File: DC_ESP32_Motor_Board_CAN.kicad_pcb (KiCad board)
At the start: 2 copper layers, 29.8 x 59.4 mm, 32 parts, among them IC1 VNH7100BASTR, IC2 TJA1050T_CM, J1 SM04B-SRSS-TB, J2 SM04B-SRSS-TB, J3 XT30PB, J4 XT30PB, J5 Conn_01x03_Pin, J6 Conn_01x02_Pin, J7 XT30PB, SW1 DSHP04TJGER, U1 MOUDLE-SEEEDUINO-XIAO-ESP32C3

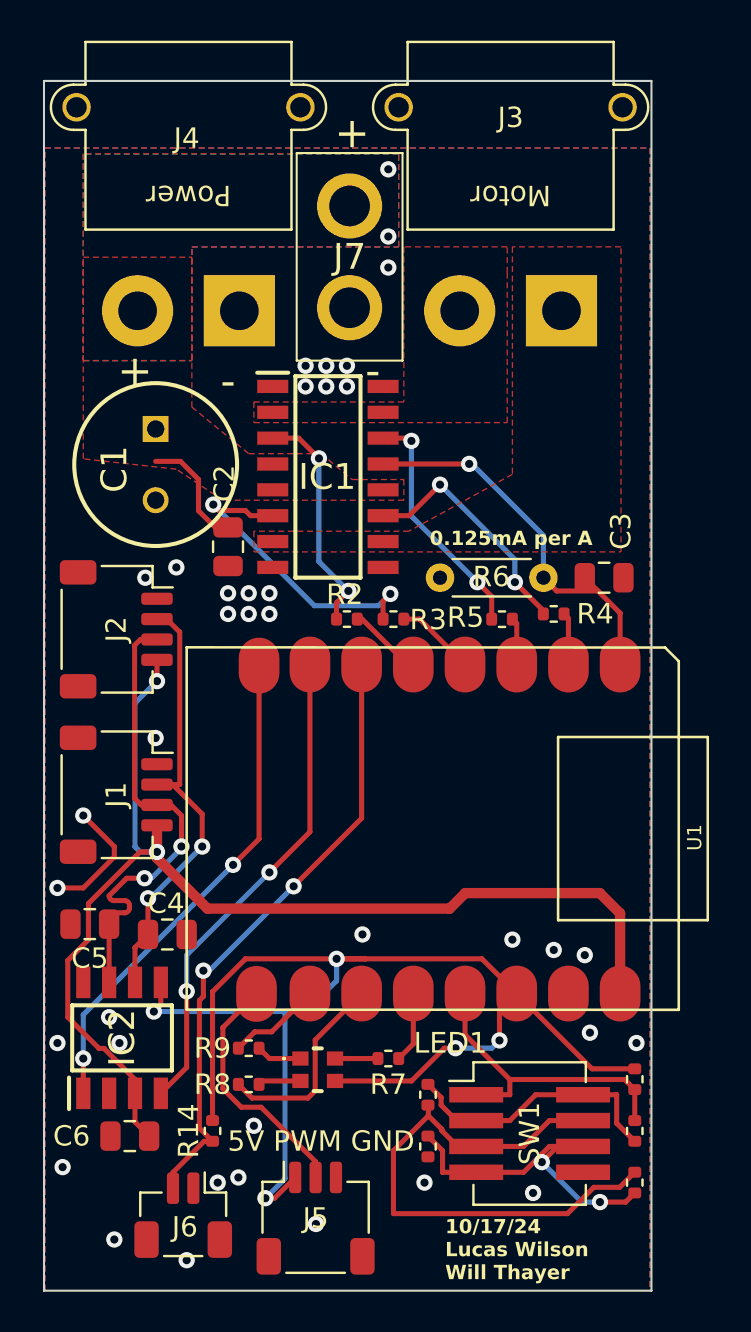
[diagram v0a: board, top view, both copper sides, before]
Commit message: Update with mounting holes
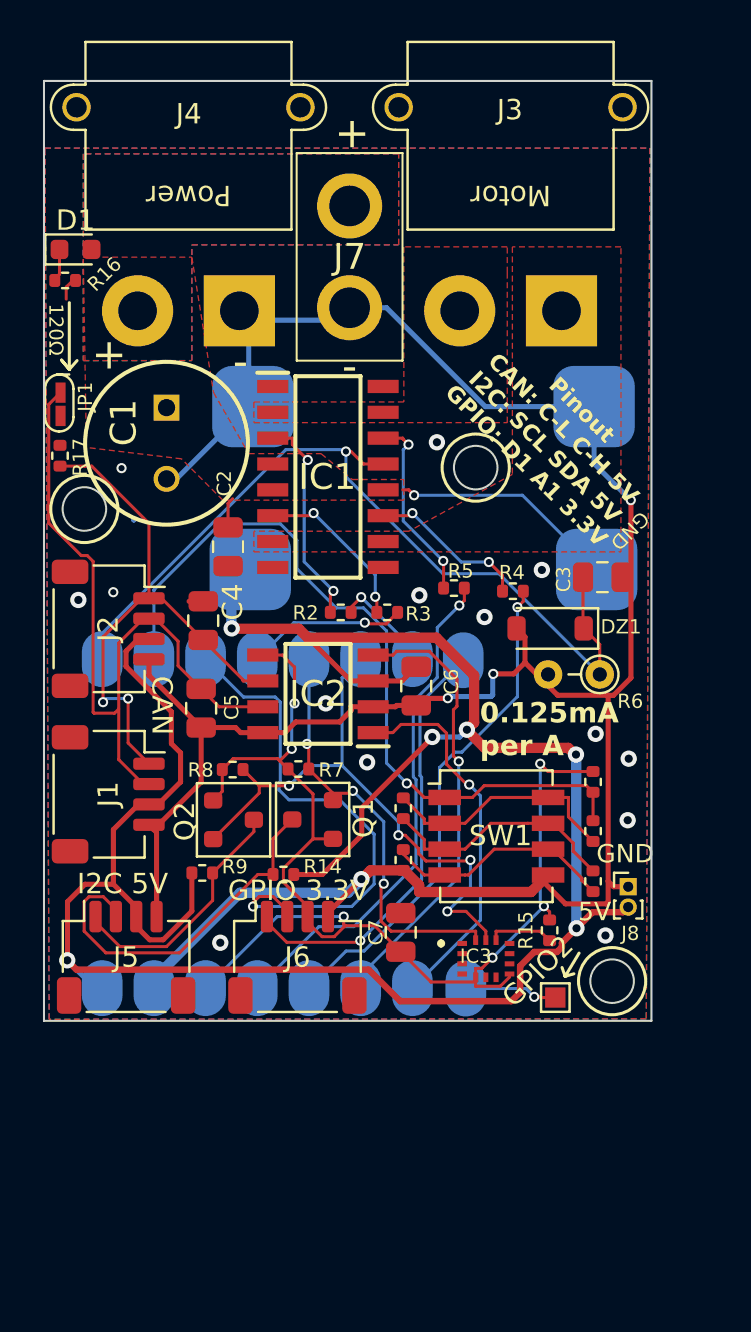
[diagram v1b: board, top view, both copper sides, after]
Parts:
- removed LED1: NH-B2020RGBA-HF, SamacSys_Parts:NHB2020RGBAHF
- added C7: 100nF, Capacitor_SMD:C_0805_2012Metric, F.Cu at (94.8, 96.2)
- added D1: KT-0603R, LED_SMD:LED_0603_1608Metric, F.Cu at (78.9, 62.6)
- added DZ1: 3.3v, Diode_SMD:D_SOD-123, F.Cu at (102.2, 81.2)
- added GPIO2: TestPoint, TestPoint:TestPoint_Pad_1.0x1.0mm, F.Cu at (102.4, 99.4)
- added IC3: LSM6DS3TR-C, SamacSys_Parts:LSM6DS3USTR, F.Cu at (99.0, 97.5)
- added J8: Conn_01x02_Pin, Connector_PinHeader_1.00mm:PinHeader_1x02_P1.00mm_Vertical, F.Cu at (106.0, 93.9)
- added JP1: SolderJumper_2_Open, Jumper:SolderJumper-2_P1.3mm_Open_RoundedPad1.0x1.5mm, F.Cu at (78.3, 70.2)
- added Q1: BSS138, PCM_Package_TO_SOT_SMD_AKL:SOT-23, F.Cu at (90.5, 90.6)
- added Q2: BSS138, PCM_Package_TO_SOT_SMD_AKL:SOT-23, F.Cu at (86.6, 90.6)
- added R15: 10k, Resistor_SMD:R_0402_1005Metric, F.Cu at (102.2, 96.1)
- added R16: 1.5k, Resistor_SMD:R_0402_1005Metric, F.Cu at (78.4, 64.1)
- added R17: 120, Resistor_SMD:R_0402_1005Metric, F.Cu at (78.1, 72.7)
- added VR1: ~, Library:EY9 reg board, B.Cu at (95.8, 73.9)
- J3, J4: footprint JST_Sorted:xt30_Right_Angle -> Library:Xt30 Horizontal
- J5: value Conn_01x03_Pin -> SM04B-SRSS-TB; footprint Connector_JST:JST_SH_SM03B-SRSS-TB_1x03-1MP_P1.00mm_Horizontal -> Connector_JST:JST_SH_SM04B-SRSS-TB_1x04-1MP_P1.00mm_Horizontal
- J6: value Conn_01x02_Pin -> SM04B-SRSS-TB; footprint Connector_JST:JST_SH_BM02B-SRSS-TB_1x02-1MP_P1.00mm_Vertical -> Connector_JST:JST_SH_SM04B-SRSS-TB_1x04-1MP_P1.00mm_Horizontal
- R14: value 8.2k -> 10k
- R6: footprint Resistor_THT:R_Axial_DIN0204_L3.6mm_D1.6mm_P5.08mm_Horizontal -> Resistor_THT:R_Axial_DIN0204_L3.6mm_D1.6mm_P2.54mm_Vertical
- R7, R8: value 120 -> 10k
- R9: value 165 -> 10k
- SW1: footprint Button_Switch_SMD:SW_DIP_SPSTx04_Slide_KingTek_DSHP04TJ_W5.25mm_P1.27mm_JPin -> Button_Switch_SMD:SW_DIP_SPSTx04_Slide_Copal_CHS-04A_W5.08mm_P1.27mm_JPin
- U1: moved to B.Cu
- moved C6 26.2 mm to (95.6, 84.1), turned to -90 degrees
- moved IC2 19.5 mm to (90.8, 84.4), turned to 180 degrees
- moved J5 15.8 mm to (81.4, 97.4)
- moved C4 15.5 mm to (85.1, 80.8), turned to -90 degrees
- moved R8 15.5 mm to (86.6, 88.2)
- moved R11 14.9 mm to (104.3, 93.7)
- moved R7 14.9 mm to (89.8, 88.1)
- moved R1 14.9 mm to (104.3, 91.2)
- moved R13 14.8 mm to (104.3, 88.8)
- moved SW1 14.7 mm to (99.5, 91.4)
- moved R12 14.1 mm to (95.0, 92.6)
- moved R10 14.1 mm to (95.0, 90.1)
- moved J6 13.9 mm to (89.8, 97.4), turned to 0 degrees
- moved R14 13.1 mm to (89.1, 93.3), turned to 0 degrees
- moved C5 11.9 mm to (85.0, 85.2), turned to -90 degrees
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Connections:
- J1 pad 1: GND -> CANL
- J1 pad 2: CANL -> CANH
- J1 pad 3: CANH -> +5V
- J1 pad 4: +5V -> GND
- J2 pad 1: GND -> CANL
- J2 pad 2: CANL -> CANH
- J2 pad 3: CANH -> +5V
- J2 pad 4: +5V -> GND
- J5 pad 1: +3.3V -> /SCL5
- J5 pad 2: ANGLE -> /SDA5
- J5 pad 3: GND -> +5V
- J6 pad 1: GND -> GPIO_1
- J6 pad 2: Button -> GPIO_A
- R14 pad 1: Button -> /SDA5
- R14 pad 2: +3.3V -> +5V
- R7 pad 1: LEDB -> SDA
- R7 pad 2: Net-(LED1-K_BLUE) -> +3.3V
- R8 pad 1: Net-(LED1-K_GREEN) -> SCL
- R8 pad 2: LEDR -> +3.3V
- R9 pad 1: Net-(LED1-K_RED) -> /SCL5
- R9 pad 2: LEDG -> +5V
- U1 pad 10: LEDG -> CANTX
- U1 pad 11: LEDR -> CANRX
- U1 pad 12: LEDB -> PWM
- U1 pad 13: DipV -> SEL
- U1 pad 2: PWM -> DipV
- U1 pad 3: SEL -> GPIO_A
- U1 pad 5: INA -> SDA
- U1 pad 6: Button -> SCL
- U1 pad 7: CANRX -> INA
- U1 pad 8: CANTX -> GPIO_1
- U1 pad 9: ANGLE -> GPIO_2
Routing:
- net GND: track 6.09 -> 129.0 mm, vias 36 -> 18
- net +5V: track 60.3 -> 115.8 mm, vias 2 -> 6
- net Button: track 30.5 -> 0.00 mm, vias 2 -> 0
- net SCL: track 0.00 -> 29.3 mm, vias 0 -> 4
- net GPIO_A: track 0.00 -> 25.9 mm, vias 0 -> 1
- net DipV: track 15.4 -> 38.3 mm, vias 0 -> 1
- net SEL: track 2.32 -> 25.0 mm, vias 0 -> 1
- net RSENSE: track 19.3 -> 42.0 mm
- net PWM: track 2.57 -> 24.6 mm, vias 0 -> 1
- net GPIO_1: track 0.00 -> 21.2 mm, vias 0 -> 1
- net SDA: track 0.00 -> 20.9 mm, vias 0 -> 3
- net /SDA5: track 0.00 -> 18.1 mm
- net Net-(R10-Pad1): track 27.5 -> 11.9 mm
- net CANH: track 23.3 -> 36.2 mm, vias 2 -> 0
- net /SCL5: track 0.00 -> 12.3 mm
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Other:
- board size 29.8 x 59.4 mm -> 29.8 x 46.2 mm
- board text added: "10/27/24 DAISY BOARD DC By Lucas Wilson & Will Thayer"
- board text added: "120Ω"
- board text added: "5V"
- board text added: "CAN"
- board text added: "GND"
- board text added: "GPIO 3.3V"
- board text added: "I2C 5V"
- board text added: "Pinout CAN: C-L C-H 5V I2C: SCL SDA 5V GPIO: D1 A1 3.3V"
- board text removed: "10/17/24 Lucas Wilson Will Thayer"
- board text removed: "5V PWM GND"
- board text removed: "WILSON FABRICATIONS"

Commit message: Last Update to PCBWAY
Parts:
- removed GPIO2: TestPoint, TestPoint:TestPoint_Pad_1.0x1.0mm
- added C8: 100nF, Capacitor_SMD:C_0805_2012Metric, F.Cu at (102.2, 98.7)
- DZ1: value 3.3v -> MM1Z3V3
- J8: value Conn_01x02_Pin -> Conn_01x03_Pin; footprint Connector_PinHeader_1.00mm:PinHeader_1x02_P1.00mm_Vertical -> Connector_PinHeader_1.00mm:PinHeader_1x03_P1.00mm_Vertical
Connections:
- J3 pad : (no net) -> GND
- J4 pad : (no net) -> GND
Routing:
- net GND: track 129.0 -> 138.2 mm, vias 18 -> 39
- net GPIO_2: track 4.58 -> 9.71 mm, vias 1 -> 0
- net +3.3V: track 58.9 -> 63.1 mm
- net Net-(JP1-A): track 0.00 -> 1.46 mm
- net +5V: track 115.8 -> 116.9 mm
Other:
- board text added: "2.2k = 2.75V at 10A"
- board text added: "GPIO2"
- board text added: "X"
- board text added: "Y"
- board text added: "Z"
